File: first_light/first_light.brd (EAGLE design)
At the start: 100 x 50 mm, 50 parts, among them IC1 MC34063AD, J1 DCJ0202, J2 DCJ0202, Q1 ZXMN4A06GTA, T1 UM2222AU3T106, T2 UM2222AU3T106, T3 UM2222AU3T106, T4 UM2222AU3T106, T5 UM2222AU3T106, U1 ESP32-WROOM-32D

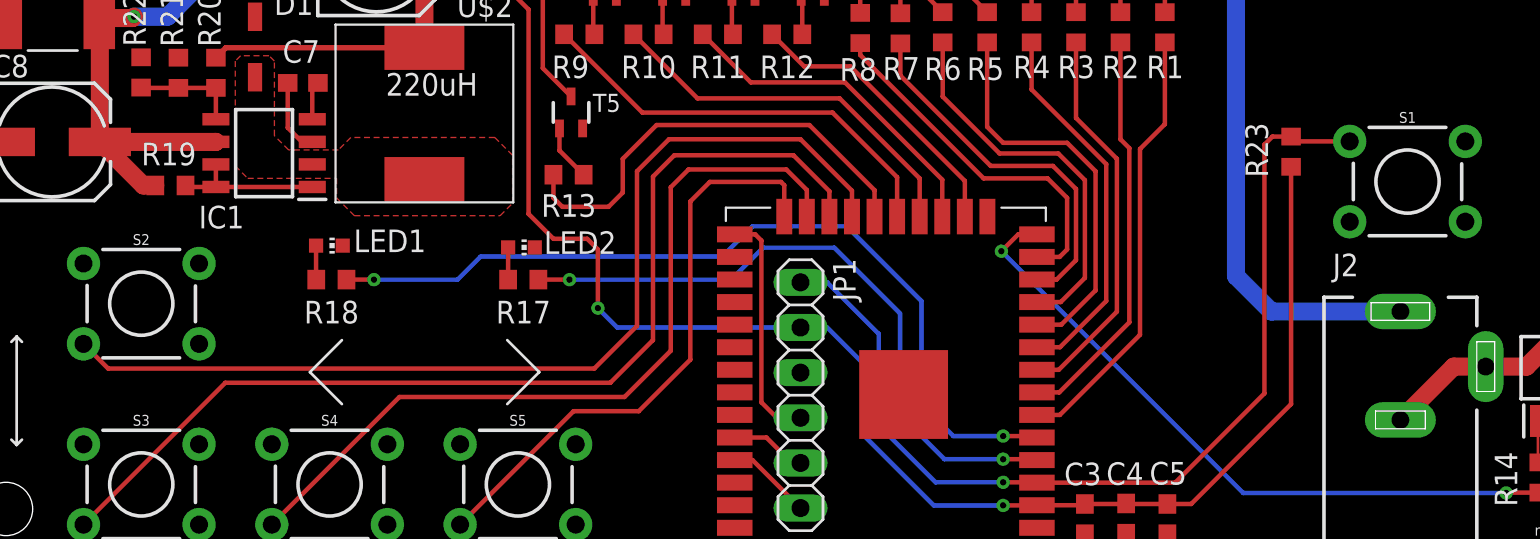
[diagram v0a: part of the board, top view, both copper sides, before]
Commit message: added MFPN and DKPN for all parts + exported BOM
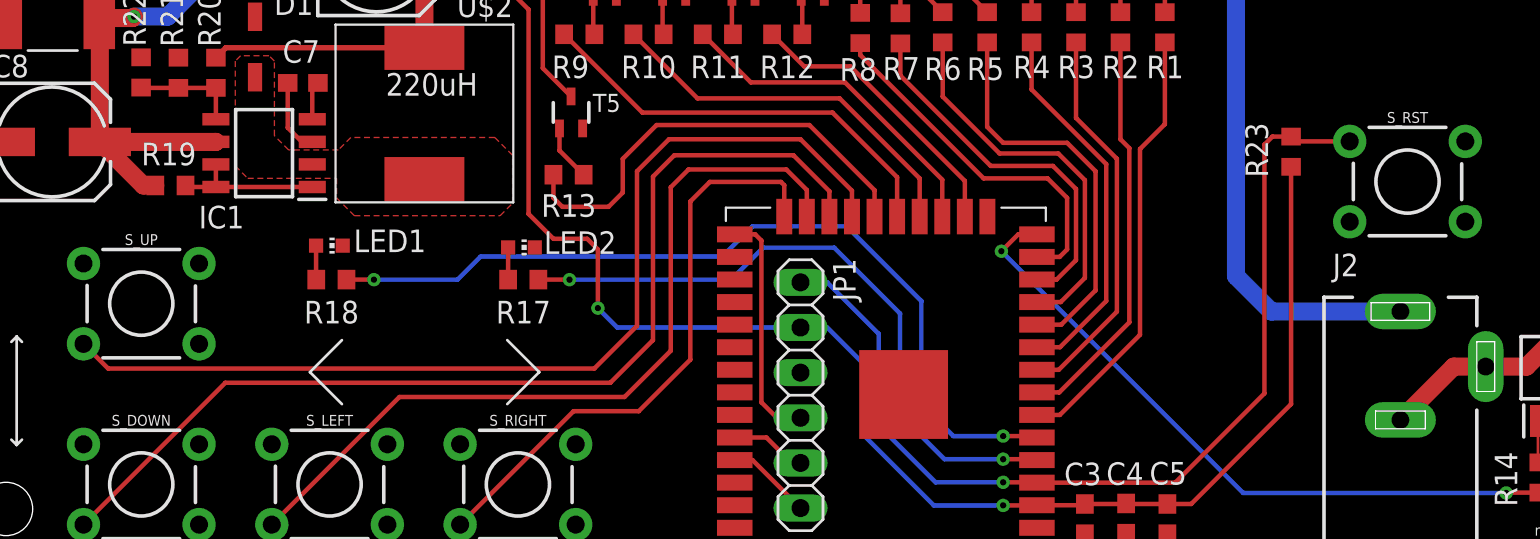
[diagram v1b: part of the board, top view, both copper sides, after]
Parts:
- C6: value 470uF -> 680uF
- LED1: value ALM -> GREEN
- LED2: value SET -> GREEN
- R1, R10, R11, R12, R13, R17, R18, R2, R3, R4, R5, R6, R7, R8, R9: value 330 -> 330R
- S_DOWN: value DOWN -> tact
- S_LEFT: value LEFT -> tact
- S_RIGHT: value RIGHT -> tact
- S_UP: value UP -> tact
- renumbered S1 to S_RST, S2 to S_UP, S3 to S_DOWN, S4 to S_LEFT, S5 to S_RIGHT
